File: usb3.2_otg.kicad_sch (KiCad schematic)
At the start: 32 parts, among them J1 USB_C_Receptacle, U2 FUSB302BMPX, U3 TPD4E05U06DQA, U4 TPD4E05U06DQA, U5 TPD4E05U06DQA

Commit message: Add files via upload
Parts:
- removed C44, C45, C46, C47, C48, C49, C50, C51, C52, C53: 100n, Capacitor_SMD:C_0201_0603Metric_Pad0.64x0.40mm_HandSolder, symbol New_Library_0:C_Small_edited
- removed D1: SMBJ5.0CA, PCM_Diode_SMD_AKL:D_SMB_TVS, symbol PCM_Diode_TVS_AKL:SMBJ5.0CA
- removed D2: PESD5V0S1BA, PCM_Diode_SMD_AKL:D_SOD-323_TVS, symbol PCM_Diode_TVS_AKL:PESD5V0S1BA
- removed R2: 10k, PCM_Resistor_SMD_AKL:R_0402_1005Metric, symbol Device:R_Small
- removed R3: 4.7k, PCM_Resistor_SMD_AKL:R_0402_1005Metric, symbol Device:R_Small
- added C170, C171, C172, C173, C174, C175, C176, C177, C178, C179: 100n, Capacitor_SMD:C_0201_0603Metric_Pad0.64x0.40mm_HandSolder, symbol New_Library_0:C_Small_edited
- added C181: 22u, Capacitor_SMD:C_0603_1608Metric, symbol New_Library_0:C_Small_edited
- added C183, C366: 1u, Capacitor_SMD:C_0402_1005Metric_Pad0.74x0.62mm_HandSolder, symbol New_Library_0:C_Small_edited
- added D20: SMBJ5.0CA, PCM_Diode_SMD_AKL:D_SMB_TVS, symbol PCM_Diode_TVS_AKL:SMBJ5.0CA
- added R46: 100k, PCM_Resistor_SMD_AKL:R_0402_1005Metric, symbol Device:R_Small
- added R58: 10k, PCM_Resistor_SMD_AKL:R_0402_1005Metric, symbol Device:R_Small
- added R61: 4.7k, PCM_Resistor_SMD_AKL:R_0402_1005Metric, symbol Device:R_Small
- added U30: ETA7014S2G, PCM_Package_TO_SOT_SMD_AKL:TSOT-23-6, symbol New_Library:ETA7014S2G
- C165: renamed from C39; value 100n -> 1u
- C166: renamed from C40; value 100n -> 1u
- C167: renamed from C41; value 100n -> 1u
- renumbered C42 to C168, C43 to C169, D3 to D10, D4 to D11, J1 to J3, R4 to R52, R5 to R53, R6 to R54, R7 to R55, R116 to R56, U3 to U4, U2 to U5, U4 to U6, U5 to U7
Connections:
- net CUSB_{OTG}_RX1_N: now also C170.2
- net CUSB_{OTG}_RX1_P: now also C171.2
- net CUSB_{OTG}_RX2_N: now also C174.2
- net CUSB_{OTG}_RX2_P: now also C175.2
- net CUSB_{OTG}_SUB1: now also R52.1, R54.1, C178.2
- net CUSB_{OTG}_SUB2: now also R53.1, R55.1, C179.2
- net CUSB_{OTG}_TX1_N: now also C172.2
- net CUSB_{OTG}_TX1_P: now also C173.2
- net CUSB_{OTG}_TX2_N: now also C176.2
- net CUSB_{OTG}_TX2_P: now also C177.2
- net GND: now also R52.2, R53.2, C181.2, C183.2, C366.2, D20.1 (K), R61.2, U30.6 (GND)
- net USB_{OTG}_PUPDCTRL1: now also R54.2
- net USB_{OTG}_PUPDCTRL2: now also R55.2
- net USB_{OTG}_RX1_N: now also C170.1
- net USB_{OTG}_RX1_P: now also C171.1
- net USB_{OTG}_RX2_N: now also C174.1
- net USB_{OTG}_RX2_P: now also C175.1
- net USB_{OTG}_SUB1: now also C178.1
- net USB_{OTG}_SUB2: now also C179.1
- net USB_{OTG}_TX1_N: now also C172.1
- net USB_{OTG}_TX1_P: now also C173.1
- net USB_{OTG}_TX2_N: now also C176.1
- net USB_{OTG}_TX2_P: now also C177.1
- net Vbus_USB_{OTG}: no longer J3.A4 (VBUS), J3.A9 (VBUS), J3.B4 (VBUS), J3.B9 (VBUS)
- net Vdet_USB_{OTG}: now also R58.2, R61.1
- net +5V renamed VCC5V0_SYS
- net SCL_USB_{OTG} renamed I2C0_SCL_M1_TP
- net SDA_USB_{OTG} renamed I2C0_SDA_M1_TP
- new net: C181.1, D20.2 (A), J3.A4 (VBUS), J3.A9 (VBUS), J3.B4 (VBUS), J3.B9 (VBUS), R46.1, U30.2 (EN), U30.4 (IN)
- new net: C366.1, R46.2, U30.5 (VCC)
- new net Vbus_USB_{PWR}: C183.1, R58.1, U30.3 (OUT)
- no-connect marks 12 -> 13
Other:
- moved on the sheet: C165, C166, C167, C168, C169, FL1, U5

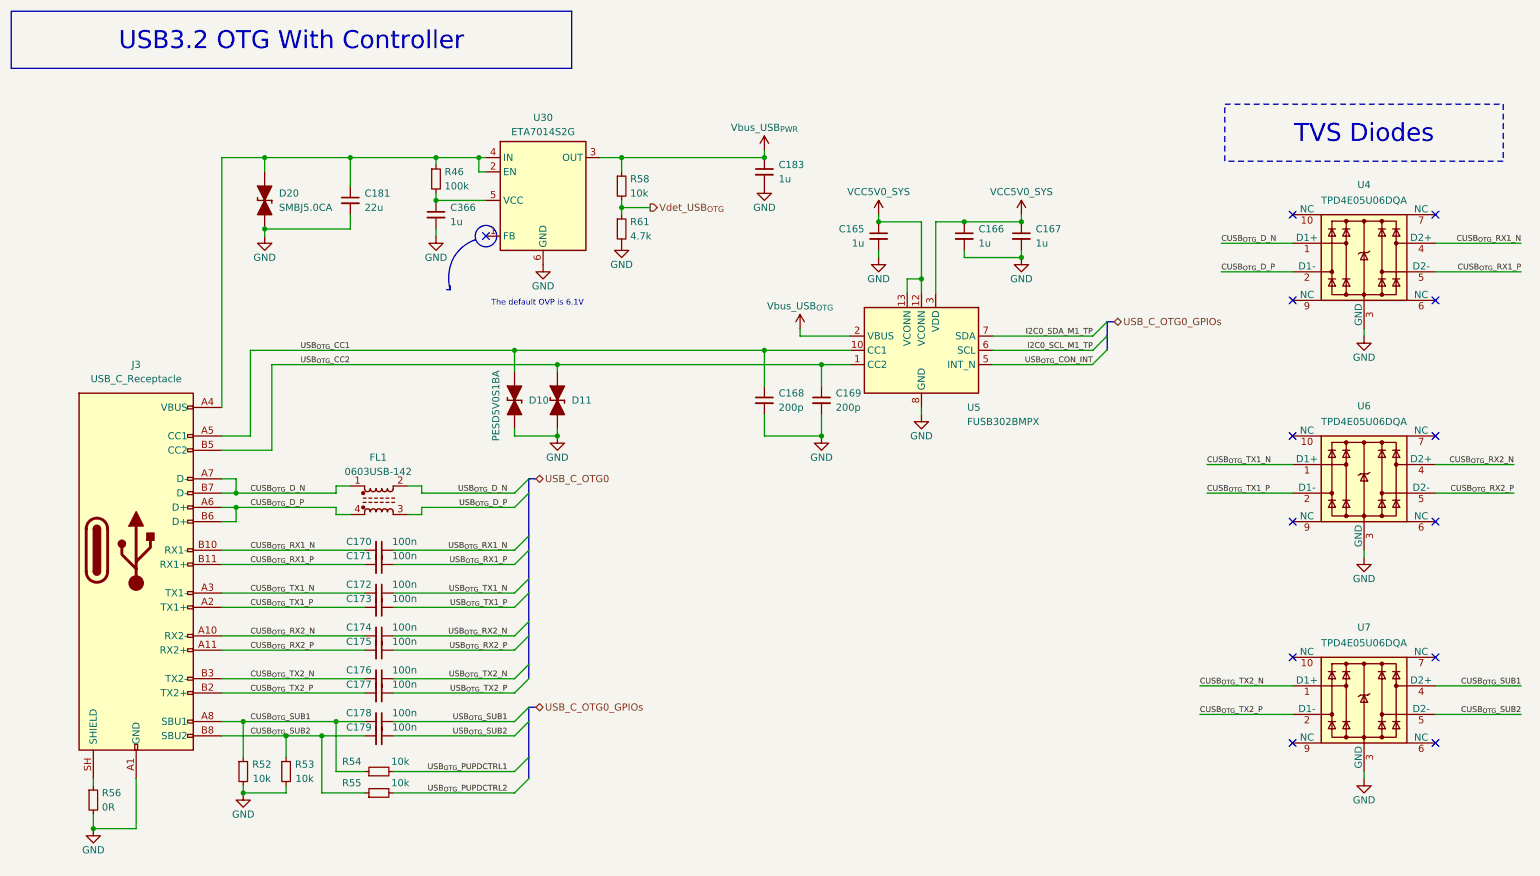
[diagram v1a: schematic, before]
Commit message: SBC Board V0.2
The SBC schematics before footprint and part number check
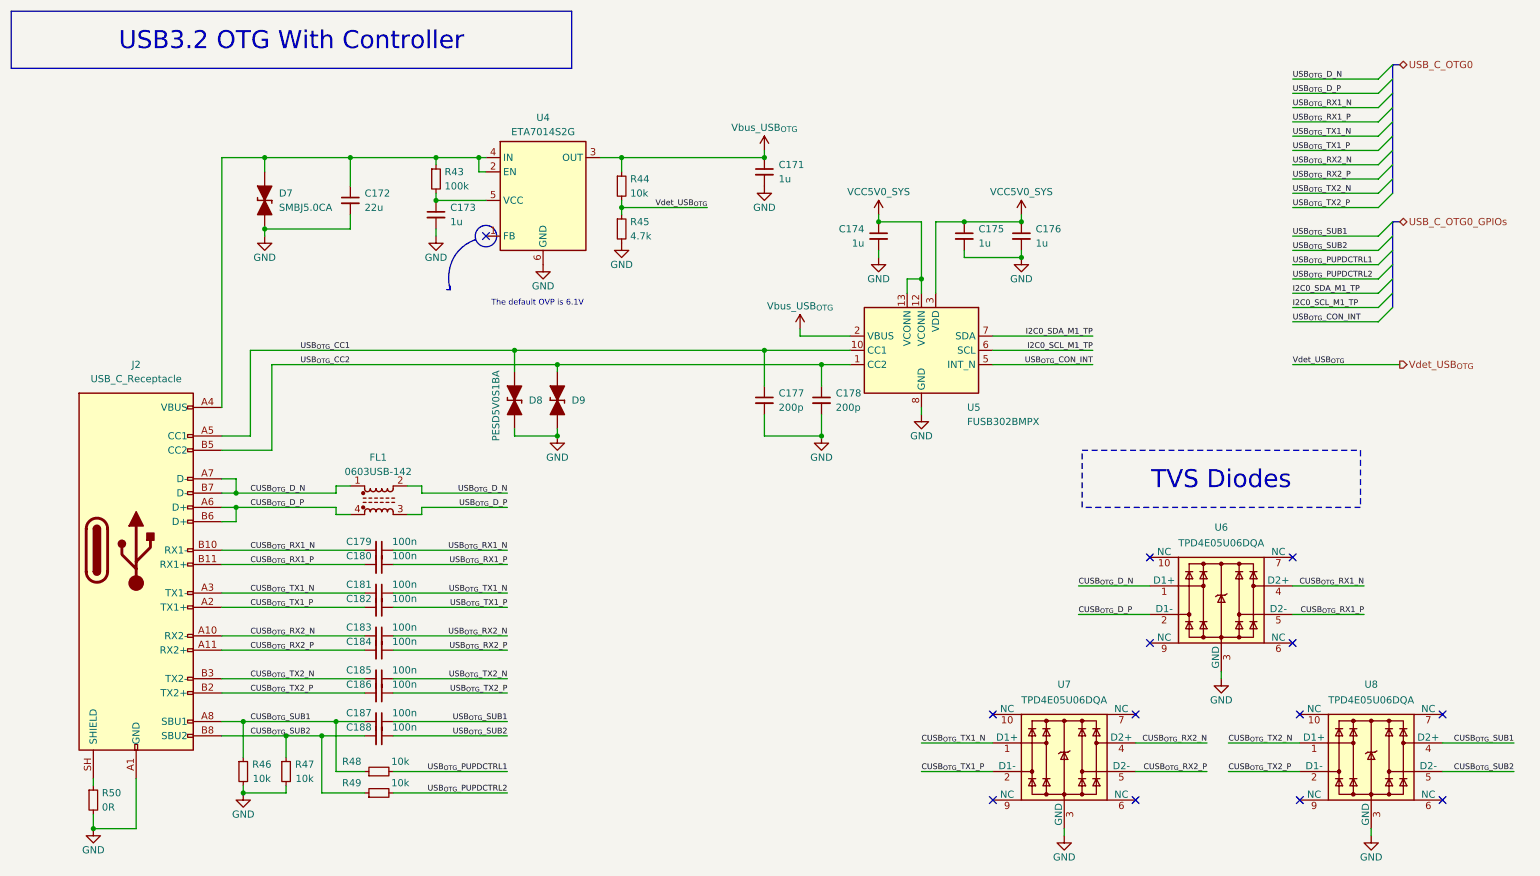
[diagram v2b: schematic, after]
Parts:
- renumbered C183 to C171, C181 to C172, C366 to C173, C165 to C174, C166 to C175, C167 to C176, C168 to C177, C169 to C178, C170 to C179, C171 to C180, C172 to C181, C173 to C182, C174 to C183, C175 to C184, C176 to C185, C177 to C186, C178 to C187, C179 to C188, D20 to D7, D10 to D8, D11 to D9, J3 to J2, R46 to R43, R58 to R44, R61 to R45, R52 to R46, R53 to R47, R54 to R48, R55 to R49, R56 to R50, U30 to U4, U4 to U6, U6 to U7, U7 to U8
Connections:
- net Vbus_USB_{PWR} is gone; now on net Vbus_USB_{OTG}: C171.1, R44.1, U4.3 (OUT)
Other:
- moved on the sheet: U6, U7, U8

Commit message: SBCv0.3
there is no big thing update just some LCSC & Mouser parts
and Big problem deleted alot of component values (:
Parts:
- removed FL1: 0603USB-142, Inductor_SMD:L_CommonModeChoke_Coilcraft_0603USB, symbol Filter:0603USB-142
- added U39: ICMEF112P900MFR, Datasheet_Footprints:ICMEF112P900MFR, symbol Datasheet_Symbols:ICMEF112P900MFR
- C171, C173: footprint Capacitor_SMD:C_0402_1005Metric_Pad0.74x0.62mm_HandSolder -> Capacitor_SMD:C_0201_0603Metric_Pad0.64x0.40mm_HandSolder; LCSC Part (none) -> C5209398; Mouser Part (none) -> CL03A105KP3NSNC
- C172: LCSC Part (none) -> C86295; Mouser Part (none) -> CL10A226MP8NUNE
- C174, C175, C176: LCSC Part (none) -> C5209398; Mouser Part (none) -> CL03A105KP3NSNC
- C177, C178: value 200p -> 200pF; LCSC Part (none) -> C325462; Mouser Part (none) -> 603-CC402JRNPO9BN201
- C179, C180, C181, C182, C183, C184, C185, C186, C187, C188: LCSC Part (none) -> C307380; Mouser Part (none) -> 187-CL03A104KO3NNNC; now left out of the parts list
- D7: LCSC Part (none) -> C113975; Mouser Part (none) -> 581-SMBJ5.0CA
- D8, D9: LCSC Part (none) -> C5158048; Mouser Part (none) -> 771-PESD5V0S1BA-T/R
- J2: footprint (none) -> Connector_USB:USB_C_Receptacle_Molex_105450-0101; LCSC Part (none) -> C134092; Mouser Part (none) -> 538-105450-0101
- R43: value 100k -> (none); LCSC Part (none) -> (show_name no)
- R44, R46, R47, R48, R49: LCSC Part (none) -> (at 0 0 0)
- R45: value 4.7k -> (none); LCSC Part (none) -> (show_name no)
- R50: value 0R -> (none); LCSC Part (none) -> )
- U4: value ETA7014S2G -> (none); Mouser Part (none) -> (pts
- U5: value FUSB302BMPX -> (none); footprint Package_DFN_QFN:WQFN-14-1EP_2.5x2.5mm_P0.5mm_EP1.45x1.45mm -> (xy -1.524 -0.508) (xy 1.524 -0.508)
- U6, U7, U8: value TPD4E05U06DQA -> (none); Mouser Part (none) -> )
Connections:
- net CUSB_{OTG}_D_N: now also U39.1 (IN1)
- net CUSB_{OTG}_D_P: now also U39.2 (IN2)
- net GND: now also U39.5 (GND), U39.6 (GND)
- net USB_{OTG}_D_N: now also U39.3 (OUT1)
- net USB_{OTG}_D_P: now also U39.4 (OUT2)
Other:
- moved on the sheet: C179, C180, C181, C182, C183, C184, C185, C186, C187, C188, R48, R49

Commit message: SBCv0.4
add LCSC & Mouser parts 
and solve the deleted value in the past version
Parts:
- R43: value (none) -> 100k; LCSC Part (show_name no) -> C60491; Mouser Part (none) -> 603-RC0402FR-07100KL
- R44, R46, R47, R48, R49: LCSC Part (at 0 0 0) -> C60490; Mouser Part (none) -> 603-RC0402FR-0710KL
- R45: value (none) -> 4.7k; LCSC Part (show_name no) -> C105871; Mouser Part (none) -> 603-RC0402FR-074K7L
- R50: value (none) -> 0R; footprint PCM_Resistor_SMD_AKL:R_0402_1005Metric_Pad0.72x0.64mm -> PCM_Resistor_SMD_AKL:R_0402_1005Metric; LCSC Part ) -> C106231; Mouser Part (none) -> 603-RC0402FR-070RL
- U4: value (none) -> ETA7014S2G; LCSC Part (none) -> C7465500; Mouser Part (pts -> (none)
- U5: value (none) -> FUSB302BMPX; footprint (xy -1.524 -0.508) (xy 1.524 -0.508) -> Package_DFN_QFN:WQFN-14-1EP_2.5x2.5mm_P0.5mm_EP1.45x1.45mm; LCSC Part (none) -> C132291; Mouser Part (none) -> 512-FUSB302BMPX
- U6, U7, U8: value (none) -> TPD4E05U06DQAR; LCSC Part (none) -> C138714; Mouser Part ) -> 595-TPD4E05U06DQAR
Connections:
- net USB_{OTG}_PUPDCTRL1: no longer R48.2
- net USB_{OTG}_PUPDCTRL2: no longer R49.2
